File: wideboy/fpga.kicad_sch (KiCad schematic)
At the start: 10 parts, among them U8 XCS20XL-TQ144

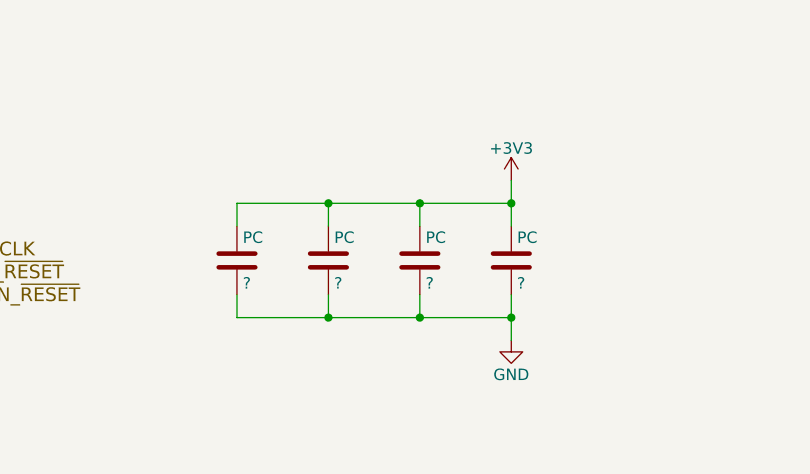
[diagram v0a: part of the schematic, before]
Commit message: Add values for capacitors and diodes
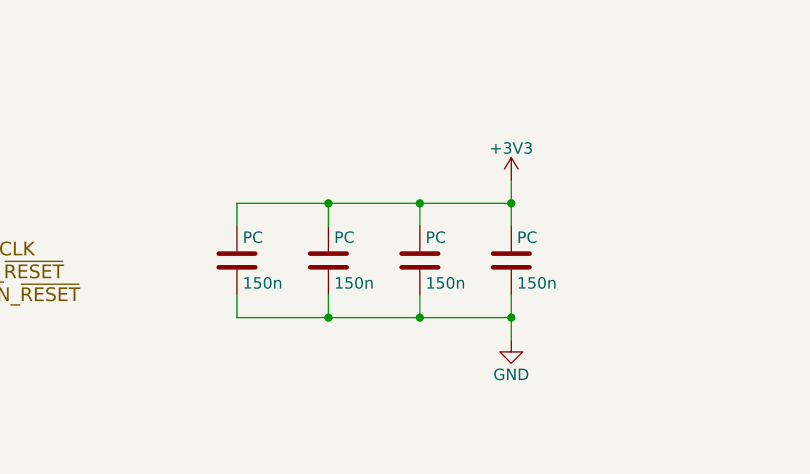
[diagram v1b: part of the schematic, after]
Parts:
- PC: value ? -> 150n
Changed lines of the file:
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@@
 	(title_block
 		(title "Wide-Boy64 AGB")
-		(date "2024-06-20")
-		(rev "2")
+		(date "2024-09-22")
+		(rev "3")
 		(company "CC-BY-SA-4.0 Michael Singer")
 		(comment 1 "https://github.com/msinger/wideboy/")
@@
 			)
 		)
-		(property "Value" "?"
+		(property "Value" "150n"
 			(at 107.315 166.37 0)
 			(effects
@@
 			)
 		)
-		(property "Value" "?"
+		(property "Value" "150n"
 			(at 117.475 166.37 0)
 			(effects
@@
 			)
 		)
-		(property "Value" "?"
+		(property "Value" "150n"
 			(at 127.635 166.37 0)
 			(effects
@@
 			)
 		)
-		(property "Value" "?"
+		(property "Value" "150n"
 			(at 137.795 166.37 0)
 			(effects
